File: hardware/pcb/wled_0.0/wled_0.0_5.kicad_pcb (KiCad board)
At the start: 2 copper layers, 139.6 x 40.7 mm, 65 parts, among them J1 Conn_01x02_Female, J2 Conn_01x03_Female, Q1 BSS138, U1 AMS1117-3.3, U2 ESP-12

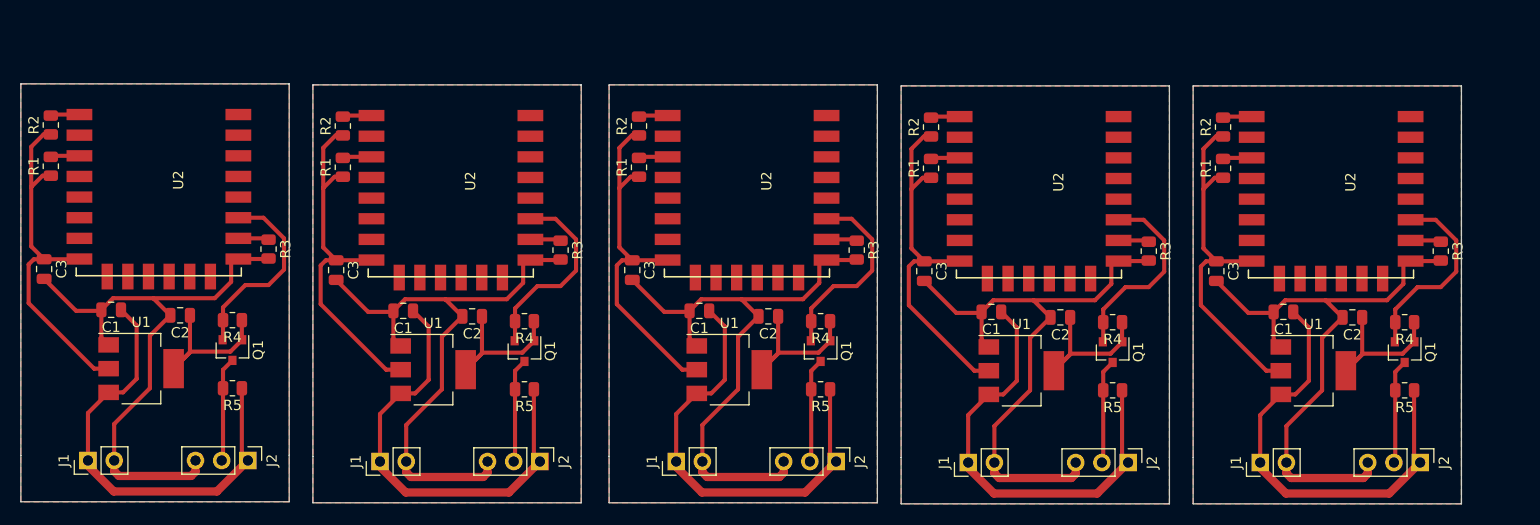
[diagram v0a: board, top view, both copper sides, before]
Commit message: правки в схеие и плате:
- заменил значения резисторов с 4к7 на 10к
- перенес некоторые дорожки дальше от края, увеличил размер площадок под сверловку
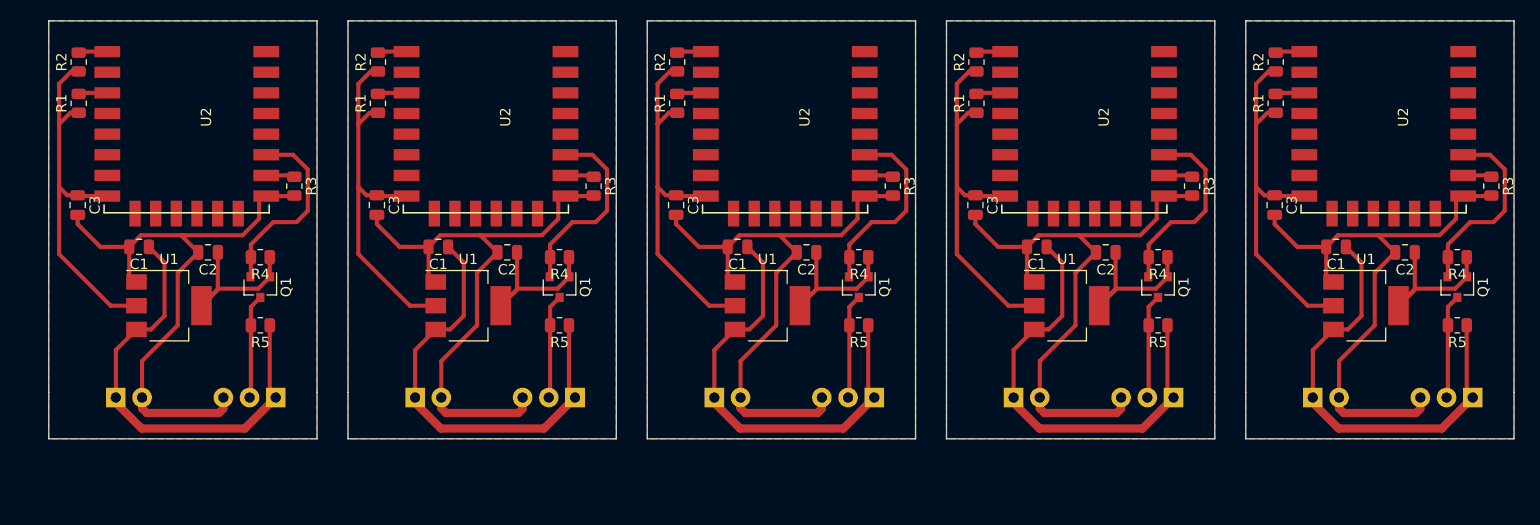
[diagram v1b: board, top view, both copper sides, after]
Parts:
- removed the C1 at (142.3, 54.1)
- removed the C1 at (114.0, 54.1)
- removed the C1 at (85.8, 54.0)
- removed the C1 at (57.0, 54.0)
- removed the C1 at (28.8, 53.9)
- removed the C2 at (149.0, 54.6)
- removed the C2 at (120.7, 54.6)
- removed the C2 at (92.4, 54.5)
- removed the C2 at (63.7, 54.5)
- removed the C2 at (35.4, 54.4)
- removed the C3 at (135.8, 50.1)
- removed the C3 at (107.5, 50.1)
- removed the C3 at (79.2, 50.0)
- removed the C3 at (50.5, 50.0)
- removed the C3 at (22.2, 50.0)
- removed the J1 at (140.1, 68.7)
- removed the J1 at (111.8, 68.7)
- removed the J1 at (83.5, 68.6)
- removed the J1 at (54.8, 68.6)
- removed the J1 at (26.5, 68.5)
- removed the J2 at (155.6, 68.7)
- removed the J2 at (127.3, 68.7)
- removed the J2 at (99.0, 68.6)
- removed the J2 at (70.3, 68.6)
- removed the J2 at (42.0, 68.5)
- removed the Q1 at (154.1, 58.0)
- removed the Q1 at (125.8, 58.0)
- removed the Q1 at (97.5, 57.9)
- removed the Q1 at (68.8, 57.9)
- removed the Q1 at (40.5, 57.8)
- removed the R1 at (136.5, 40.2)
- removed the R1 at (108.2, 40.2)
- removed the R1 at (79.9, 40.1)
- removed the R1 at (51.2, 40.1)
- removed the R1 at (22.9, 40.0)
- removed the R2 at (136.5, 36.2)
- removed the R2 at (108.2, 36.2)
- removed the R2 at (79.9, 36.1)
- removed the R2 at (51.2, 36.1)
- removed the R2 at (22.9, 36.0)
- removed the R3 at (157.6, 48.2)
- removed the R3 at (129.3, 48.2)
- removed the R3 at (101.0, 48.1)
- removed the R3 at (72.3, 48.1)
- removed the R3 at (44.0, 48.0)
- removed the R4 at (154.1, 55.1)
- removed the R4 at (125.8, 55.1)
- removed the R4 at (97.5, 55.0)
- removed the R4 at (68.8, 55.0)
- removed the R4 at (40.5, 54.9)
- removed the R5 at (154.1, 61.7)
- removed the R5 at (125.8, 61.7)
- removed the R5 at (97.5, 61.6)
- removed the R5 at (68.8, 61.6)
- removed the R5 at (40.5, 61.5)
- removed the U1 at (145.2, 59.8)
- removed the U1 at (117.0, 59.8)
- removed the U1 at (88.7, 59.7)
- removed the U1 at (60.0, 59.7)
- removed the U1 at (31.6, 59.6)
- removed the U2 at (140.0, 35.2)
- removed the U2 at (111.7, 35.2)
- removed the U2 at (83.4, 35.1)
- removed the U2 at (54.7, 35.1)
- removed the U2 at (26.4, 35.0)
- added C1: 100, Capacitor_SMD:C_0805_2012Metric, F.Cu at (147.4, 47.8)
- added C1: 100, Capacitor_SMD:C_0805_2012Metric, F.Cu at (118.5, 47.8)
- added C1: 100, Capacitor_SMD:C_0805_2012Metric, F.Cu at (89.5, 47.8)
- added C1: 100, Capacitor_SMD:C_0805_2012Metric, F.Cu at (60.5, 47.8)
- added C1: 100, Capacitor_SMD:C_0805_2012Metric, F.Cu at (31.4, 47.8)
- added C2: 100, Capacitor_SMD:C_0805_2012Metric, F.Cu at (154.1, 48.3)
- added C2: 100, Capacitor_SMD:C_0805_2012Metric, F.Cu at (125.1, 48.3)
- added C2: 100, Capacitor_SMD:C_0805_2012Metric, F.Cu at (96.1, 48.3)
- added C2: 100, Capacitor_SMD:C_0805_2012Metric, F.Cu at (67.1, 48.3)
- added C2: 100, Capacitor_SMD:C_0805_2012Metric, F.Cu at (38.1, 48.3)
- added C3: 100, Capacitor_SMD:C_0805_2012Metric, F.Cu at (141.5, 43.8)
- added C3: 100, Capacitor_SMD:C_0805_2012Metric, F.Cu at (112.5, 43.8)
- added C3: 100, Capacitor_SMD:C_0805_2012Metric, F.Cu at (83.5, 43.8)
- added C3: 100, Capacitor_SMD:C_0805_2012Metric, F.Cu at (54.5, 43.8)
- added C3: 100, Capacitor_SMD:C_0805_2012Metric, F.Cu at (25.5, 43.8)
- added J1: Conn_01x02_Female, Connector_PinHeader_2.54mm:PinHeader_1x02_P2.54mm_Horizontal, B.Cu at (145.2, 62.4)
- added J1: Conn_01x02_Female, Connector_PinHeader_2.54mm:PinHeader_1x02_P2.54mm_Horizontal, B.Cu at (116.2, 62.4)
- added J1: Conn_01x02_Female, Connector_PinHeader_2.54mm:PinHeader_1x02_P2.54mm_Horizontal, B.Cu at (87.2, 62.4)
- added J1: Conn_01x02_Female, Connector_PinHeader_2.54mm:PinHeader_1x02_P2.54mm_Horizontal, B.Cu at (58.2, 62.4)
- added J1: Conn_01x02_Female, Connector_PinHeader_2.54mm:PinHeader_1x02_P2.54mm_Horizontal, B.Cu at (29.2, 62.4)
- added J2: Conn_01x03_Female, Connector_PinHeader_2.54mm:PinHeader_1x03_P2.54mm_Horizontal, B.Cu at (160.7, 62.4)
- added J2: Conn_01x03_Female, Connector_PinHeader_2.54mm:PinHeader_1x03_P2.54mm_Horizontal, B.Cu at (131.7, 62.4)
- added J2: Conn_01x03_Female, Connector_PinHeader_2.54mm:PinHeader_1x03_P2.54mm_Horizontal, B.Cu at (102.7, 62.4)
- added J2: Conn_01x03_Female, Connector_PinHeader_2.54mm:PinHeader_1x03_P2.54mm_Horizontal, B.Cu at (73.7, 62.4)
- added J2: Conn_01x03_Female, Connector_PinHeader_2.54mm:PinHeader_1x03_P2.54mm_Horizontal, B.Cu at (44.7, 62.4)
- added Q1: BSS138, Package_TO_SOT_SMD:SOT-23, F.Cu at (159.2, 51.7)
- added Q1: BSS138, Package_TO_SOT_SMD:SOT-23, F.Cu at (130.2, 51.7)
- added Q1: BSS138, Package_TO_SOT_SMD:SOT-23, F.Cu at (101.2, 51.7)
- added Q1: BSS138, Package_TO_SOT_SMD:SOT-23, F.Cu at (72.2, 51.7)
- added Q1: BSS138, Package_TO_SOT_SMD:SOT-23, F.Cu at (43.2, 51.7)
- added R1: 4k7, Resistor_SMD:R_0805_2012Metric, F.Cu at (141.6, 33.9)
- added R1: 4k7, Resistor_SMD:R_0805_2012Metric, F.Cu at (112.6, 33.9)
- added R1: 4k7, Resistor_SMD:R_0805_2012Metric, F.Cu at (83.6, 33.9)
- added R1: 4k7, Resistor_SMD:R_0805_2012Metric, F.Cu at (54.6, 33.9)
- added R1: 4k7, Resistor_SMD:R_0805_2012Metric, F.Cu at (25.6, 33.9)
- added R2: 4k7, Resistor_SMD:R_0805_2012Metric, F.Cu at (141.6, 29.9)
- added R2: 4k7, Resistor_SMD:R_0805_2012Metric, F.Cu at (112.6, 29.9)
- added R2: 4k7, Resistor_SMD:R_0805_2012Metric, F.Cu at (83.6, 29.9)
- added R2: 4k7, Resistor_SMD:R_0805_2012Metric, F.Cu at (54.6, 29.9)
- added R2: 4k7, Resistor_SMD:R_0805_2012Metric, F.Cu at (25.6, 29.9)
- added R3: 4k7, Resistor_SMD:R_0805_2012Metric, F.Cu at (162.5, 41.9)
- added R3: 4k7, Resistor_SMD:R_0805_2012Metric, F.Cu at (133.5, 41.9)
- added R3: 4k7, Resistor_SMD:R_0805_2012Metric, F.Cu at (104.5, 41.9)
- added R3: 4k7, Resistor_SMD:R_0805_2012Metric, F.Cu at (75.5, 41.9)
- added R3: 4k7, Resistor_SMD:R_0805_2012Metric, F.Cu at (46.5, 41.9)
- added R4: 10k, Resistor_SMD:R_0805_2012Metric, F.Cu at (159.2, 48.8)
- added R4: 10k, Resistor_SMD:R_0805_2012Metric, F.Cu at (130.2, 48.8)
- added R4: 10k, Resistor_SMD:R_0805_2012Metric, F.Cu at (101.2, 48.8)
- added R4: 10k, Resistor_SMD:R_0805_2012Metric, F.Cu at (72.2, 48.8)
- added R4: 10k, Resistor_SMD:R_0805_2012Metric, F.Cu at (43.2, 48.8)
- added R5: 10k, Resistor_SMD:R_0805_2012Metric, F.Cu at (159.2, 55.4)
- added R5: 10k, Resistor_SMD:R_0805_2012Metric, F.Cu at (130.2, 55.4)
- added R5: 10k, Resistor_SMD:R_0805_2012Metric, F.Cu at (101.2, 55.4)
- added R5: 10k, Resistor_SMD:R_0805_2012Metric, F.Cu at (72.2, 55.4)
- added R5: 10k, Resistor_SMD:R_0805_2012Metric, F.Cu at (43.2, 55.4)
- added U1: AMS1117-3.3, Package_TO_SOT_SMD:SOT-223-3_TabPin2, F.Cu at (150.3, 53.5)
- added U1: AMS1117-3.3, Package_TO_SOT_SMD:SOT-223-3_TabPin2, F.Cu at (121.3, 53.5)
- added U1: AMS1117-3.3, Package_TO_SOT_SMD:SOT-223-3_TabPin2, F.Cu at (92.3, 53.5)
- added U1: AMS1117-3.3, Package_TO_SOT_SMD:SOT-223-3_TabPin2, F.Cu at (63.4, 53.5)
- added U1: AMS1117-3.3, Package_TO_SOT_SMD:SOT-223-3_TabPin2, F.Cu at (34.4, 53.5)
- added U2: ESP-12, esp8266:ESP-12E_SMD, F.Cu at (145.1, 28.9)
- added U2: ESP-12, esp8266:ESP-12E_SMD, F.Cu at (116.1, 28.9)
- added U2: ESP-12, esp8266:ESP-12E_SMD, F.Cu at (87.1, 28.9)
- added U2: ESP-12, esp8266:ESP-12E_SMD, F.Cu at (58.1, 28.9)
- added U2: ESP-12, esp8266:ESP-12E_SMD, F.Cu at (29.1, 28.9)
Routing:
- net (no net): track 0.00 -> 978.4 mm
- net GND: track 297.5 -> 0.00 mm
- net Net-(C2-Pad1): track 259.7 -> 0.00 mm
- net +5V: track 217.6 -> 0.00 mm
- net Net-(Q1-Pad2): track 97.8 -> 0.00 mm
- net Net-(J2-Pad2): track 50.7 -> 0.00 mm
- net Net-(R3-Pad1): track 18.4 -> 0.00 mm
- net Net-(R2-Pad2): track 17.6 -> 0.00 mm
- net Net-(R1-Pad2): track 17.6 -> 0.00 mm
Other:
- board size 139.6 x 40.7 mm -> 142 x 40.5 mm
